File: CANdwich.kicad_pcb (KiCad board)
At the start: 2 copper layers, 22 x 48 mm, 49 parts, among them J1 DE9_Receptacle, J2 USB_C_Receptacle_USB2.0, J4 Conn_01x04_Socket, U1 AP2127K-3.3, U2 STM32F072CBT6, U3 SN6505BDBV, U4 AP2204K-5.0TRG1, U6 ISO1050DUB, Y1 16MHz

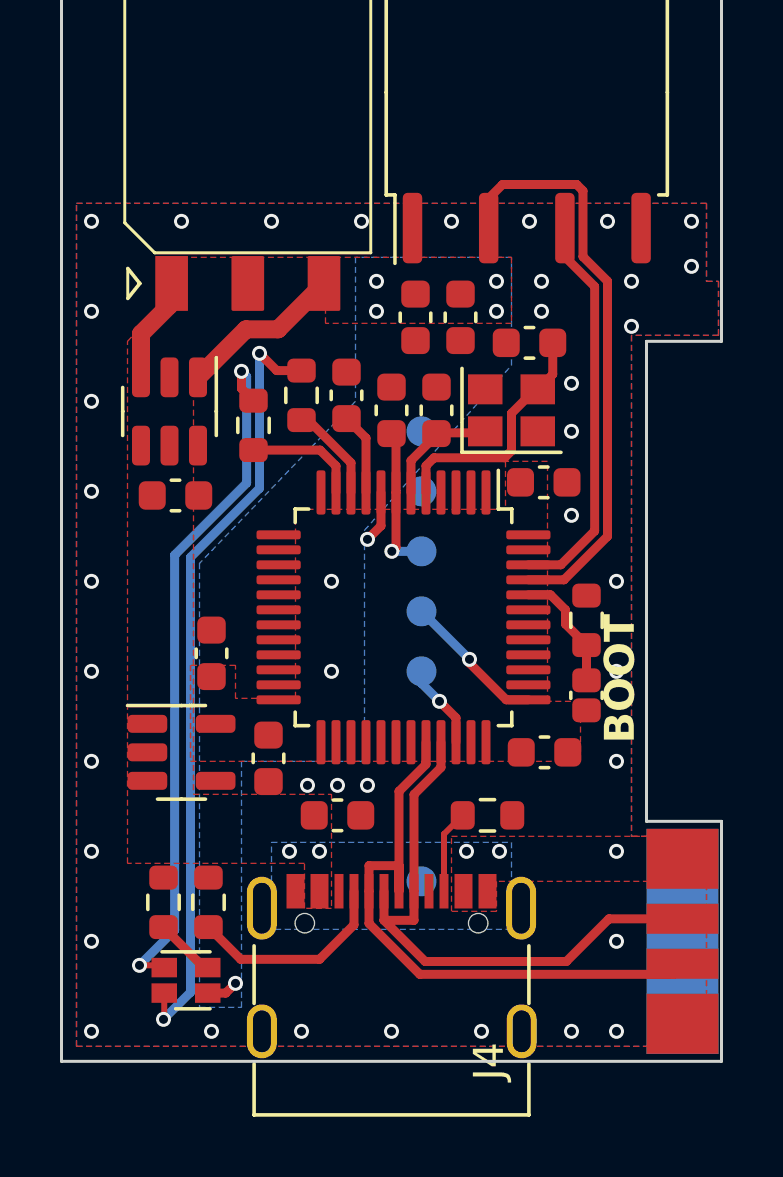
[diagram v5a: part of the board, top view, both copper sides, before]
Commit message: Change indication LED
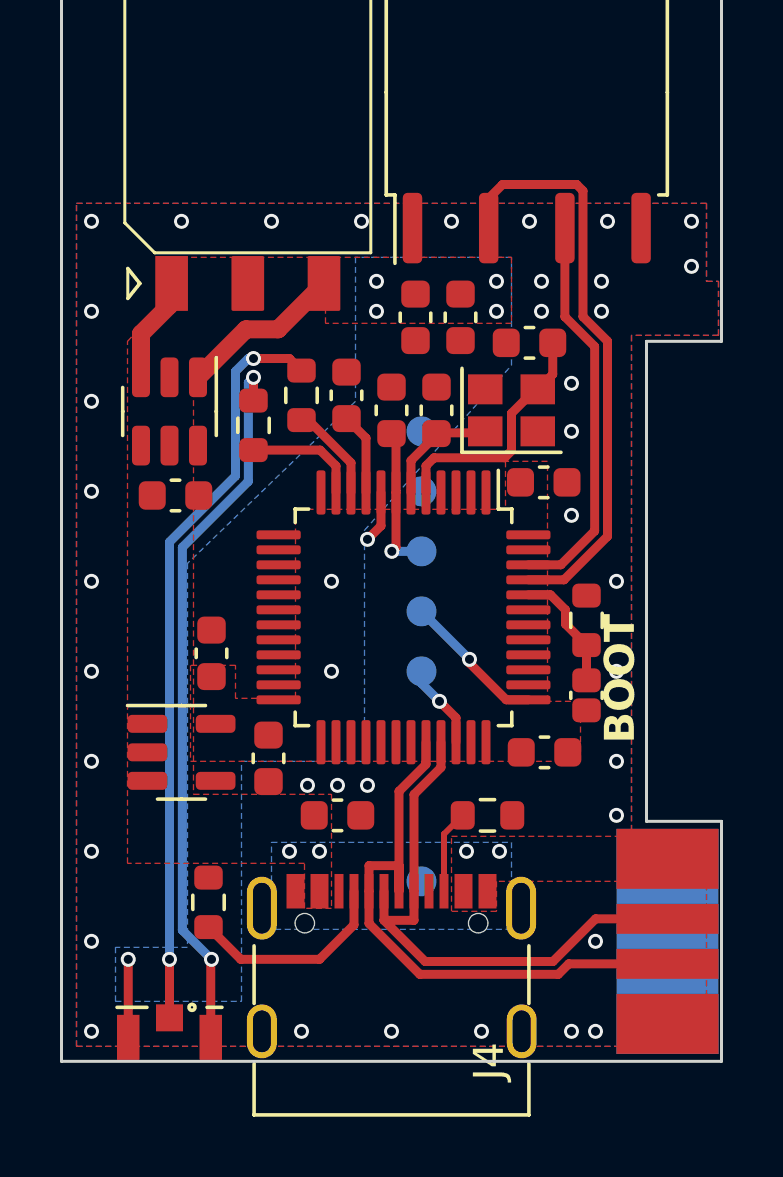
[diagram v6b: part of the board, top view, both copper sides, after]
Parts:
- removed D2: LED_RGBA, LED_SMD:LED_LiteOn_LTST-C19HE1WT
- removed R6: 150, Resistor_SMD:R_0603_1608Metric
- added D1: LTST-S326KGJRKT_RG, 0_terry:LED_LiteOn_LTST-S326, F.Cu at (160.6, 109.1)
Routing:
- net Net-(D2-BK): track 2.03 -> 0.00 mm
- net VD3V3: track 3.79 -> 5.33 mm
- net Net-(D1-K2): track 26.0 -> 25.0 mm
- net Net-(D1-K1): track 23.3 -> 24.2 mm
- net /USB_D-: track 20.5 -> 19.9 mm
- net /USB_D+: track 19.4 -> 18.9 mm
- net Earth: vias 40 -> 39
